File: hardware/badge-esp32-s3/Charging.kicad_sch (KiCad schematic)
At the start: 0 parts

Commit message: Make progress on charger, switch out some diodes
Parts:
- added D10: DSK24, PCM_JLCPCB:D_SOD-123FL, symbol PCM_JLCPCB-Diodes:Schottky,DSK24
- added J4: LiPo, Connector_JST:JST_PH_S2B-PH-K_1x02_P2.00mm_Horizontal, symbol Connector_Generic:Conn_01x02
- added Q3: HL2301A, PCM_JLCPCB:Q_SOT-23, symbol PCM_JLCPCB-Transistors:PMOS,HL2301A
- added R19: 100kΩ, PCM_JLCPCB:R_0402, symbol PCM_JLCPCB-Resistors:0402,100kΩ
- added U4: TP4056, PCM_JLCPCB:ESOP-8_L4.9-W3.9-P1.27-LS6.0-BL-EP, symbol PCM_JLCPCB-Power:Battery, Li-Ion, 1.0A, TP4056
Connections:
- new net GND: J4.2 (Pin_2), R19.1, U4.1 (TEMP), U4.3 (GND)
- new net USB_1: D10.2, Q3.1 (G), R19.2, U4.4 (VCC)
- new net VBATT: J4.1 (Pin_1), Q3.3 (D), U4.5 (BAT)
- new net VOUT: D10.1, Q3.2 (S)

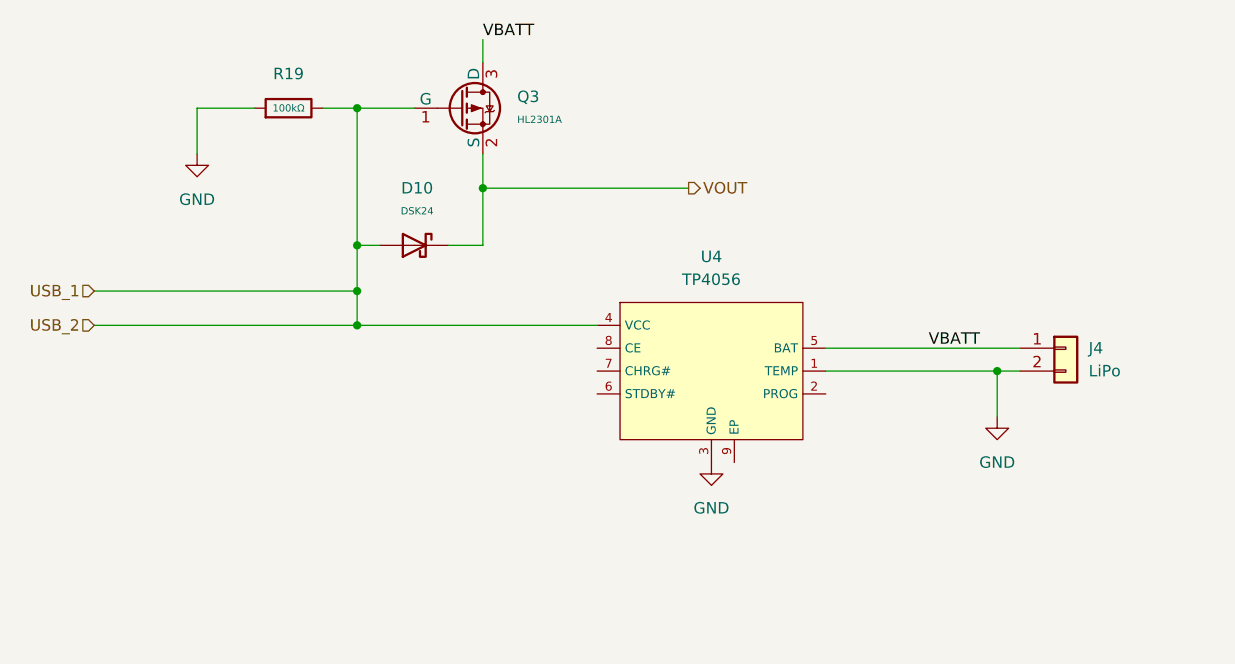
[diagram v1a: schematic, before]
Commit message: Finish charging circuit Switched out schottky diodes Better linear regulator
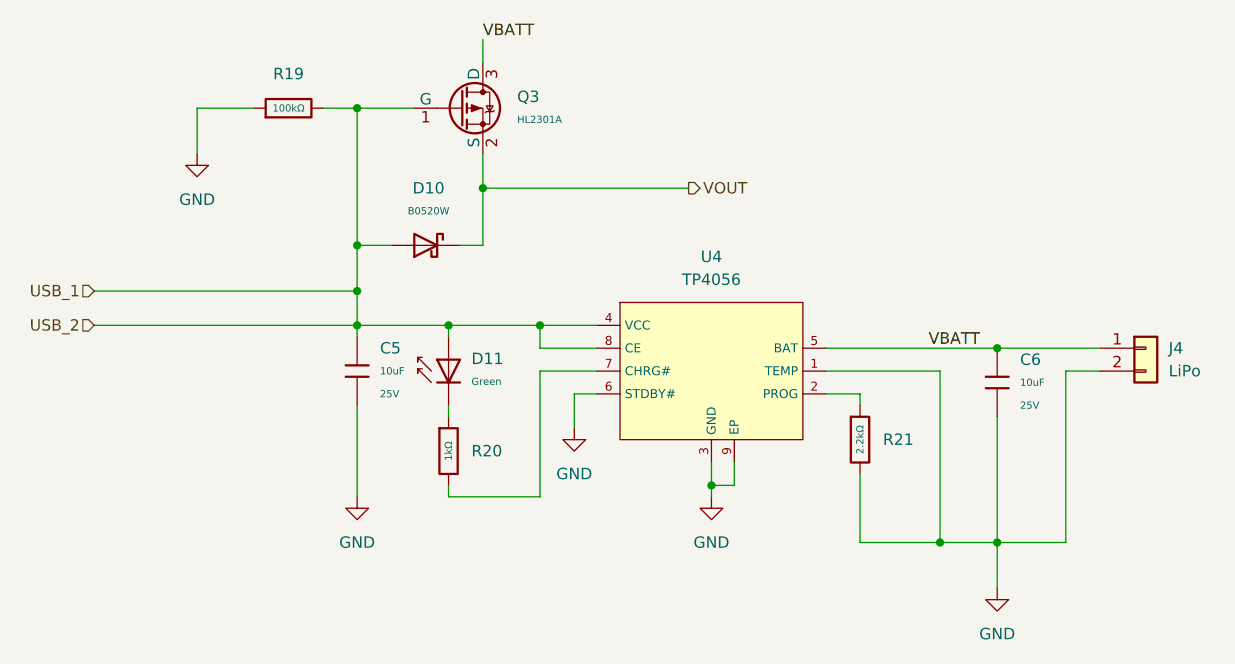
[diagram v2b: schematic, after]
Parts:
- removed D10: DSK24, PCM_JLCPCB:D_SOD-123FL, symbol PCM_JLCPCB-Diodes:Schottky,DSK24
- added C5, C6: 10uF, PCM_JLCPCB:C_0603, symbol PCM_JLCPCB-Capacitors:0603,10uF,(2)
- added D10: B0520W, PCM_JLCPCB:D_SOD-123, symbol PCM_JLCPCB-Diodes:Schottky,B0520W
- added D11: Green, PCM_JLCPCB:D_0805, symbol PCM_JLCPCB-Diodes:LED,0805,Green
- added R20: 1kΩ, PCM_JLCPCB:R_0402, symbol PCM_JLCPCB-Resistors:0402,1kΩ
- added R21: 2.2kΩ, PCM_JLCPCB:R_0402, symbol PCM_JLCPCB-Resistors:0402,2.2kΩ
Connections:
- net GND: now also U4.6 (STDBY#), U4.9 (EP), C5.2, C6.2, R21.2
- net USB_1: now also U4.8 (CE), C5.1, D10.2, D11.2
- net VBATT: now also C6.1
- net VOUT: now also D10.1
- net at U4.2 (PROG): now also R21.1
- net at U4.7 (CHRG#): now also R20.2
- new net: D11.1, R20.1
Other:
- moved on the sheet: J4
